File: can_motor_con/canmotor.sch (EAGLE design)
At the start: 36 parts

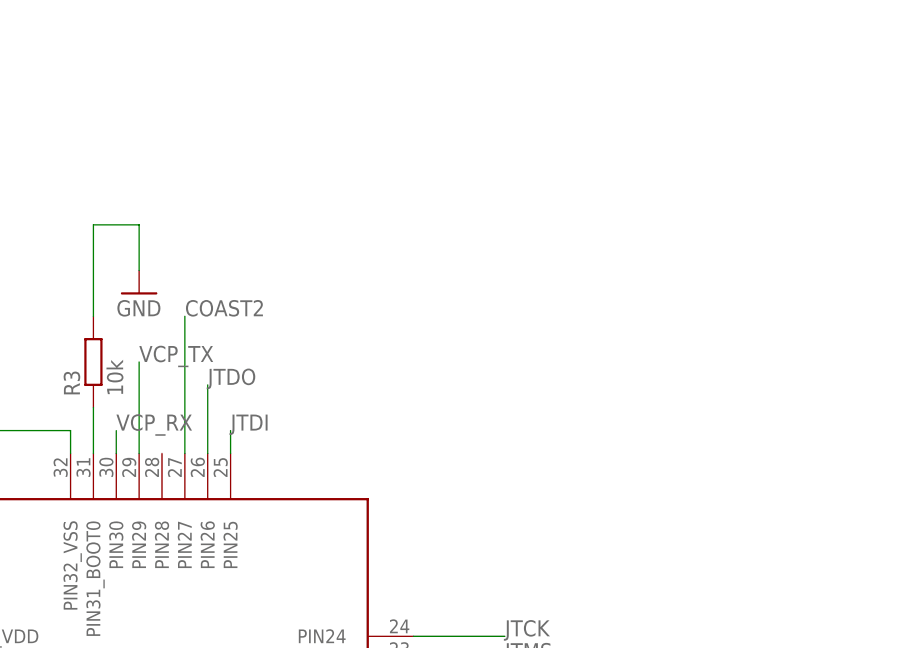
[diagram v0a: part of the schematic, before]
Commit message: ledをついか
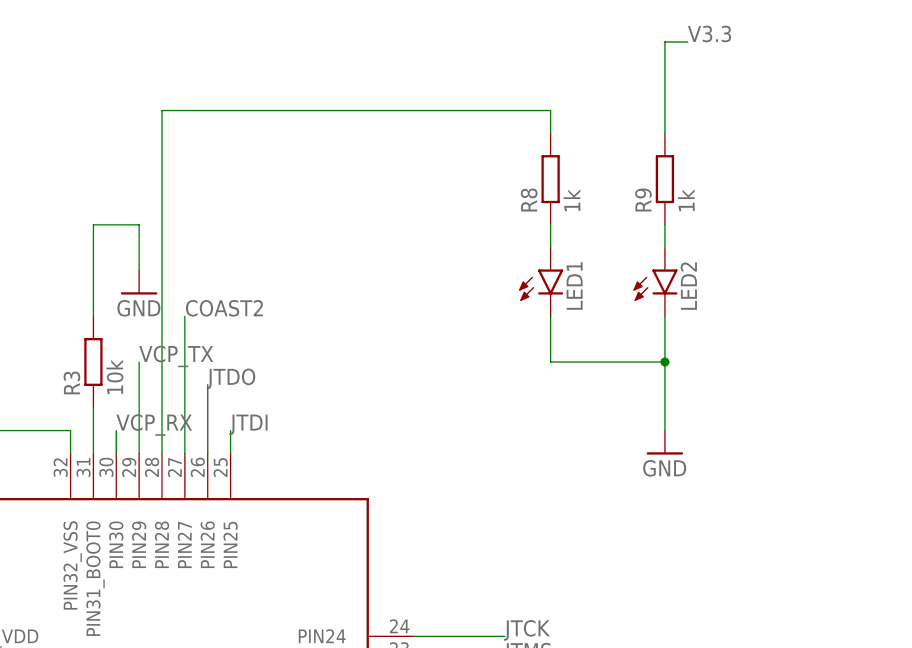
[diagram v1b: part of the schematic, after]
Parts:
- added LED1, LED2: (no value), user_leds:1608LED
- added R8, R9: 1k, user_rcl:R_REG
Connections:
- new net N$11: LED1.A, R8.1
- new net N$12: LED2.A, R9.1
- new net N$14: R8.2, U$1.PIN28
- net GND: now also LED1.K, LED2.K
- net V3.3: now also R9.2
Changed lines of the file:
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@@
 <part name="C12" library="rcl" library_urn="urn:adsk.eagle:library:334" deviceset="C-EU" device="C1608" package3d_urn="urn:adsk.eagle:package:23621/2" value="0.1u"/>
 <part name="C13" library="rcl" library_urn="urn:adsk.eagle:library:334" deviceset="C-EU" device="C1608" package3d_urn="urn:adsk.eagle:package:23621/2" value="0.1u"/>
+<part name="LED1" library="user_leds" deviceset="1608LED" device=""/>
+<part name="LED2" library="user_leds" deviceset="1608LED" device=""/>
+<part name="R8" library="user_rcl" deviceset="R_REG" device="" value="1k"/>
+<part name="R9" library="user_rcl" deviceset="R_REG" device="" value="1k"/>
+<part name="GND10" library="supply1" library_urn="urn:adsk.eagle:library:371" deviceset="GND" device=""/>
 </parts>
 <sheets>
@@
 <attribute name="NAME" x="392.176" y="35.179" size="1.778" layer="95" rot="R180"/>
 <attribute name="VALUE" x="392.176" y="40.259" size="1.778" layer="96" rot="R180"/>
+</instance>
+<instance part="LED1" gate="G$1" x="274.32" y="152.4" smashed="yes">
+<attribute name="NAME" x="277.876" y="147.828" size="1.778" layer="95" rot="R90"/>
+<attribute name="VALUE" x="280.035" y="147.828" size="1.778" layer="96" rot="R90"/>
+</instance>
+<instance part="LED2" gate="G$1" x="287.02" y="152.4" smashed="yes">
+<attribute name="NAME" x="290.576" y="147.828" size="1.778" layer="95" rot="R90"/>
+<attribute name="VALUE" x="292.735" y="147.828" size="1.778" layer="96" rot="R90"/>
+</instance>
+<instance part="R8" gate="G$1" x="274.32" y="162.56" smashed="yes" rot="R90">
+<attribute name="NAME" x="272.8214" y="158.75" size="1.778" layer="95" rot="R90"/>
+<attribute name="VALUE" x="277.622" y="158.75" size="1.778" layer="96" rot="R90"/>
+</instance>
+<instance part="R9" gate="G$1" x="287.02" y="162.56" smashed="yes" rot="R90">
+<attribute name="NAME" x="285.5214" y="158.75" size="1.778" layer="95" rot="R90"/>
+<attribute name="VALUE" x="290.322" y="158.75" size="1.778" layer="96" rot="R90"/>
+</instance>
+<instance part="GND10" gate="1" x="287.02" y="132.08" smashed="yes">
+<attribute name="VALUE" x="284.48" y="129.54" size="1.778" layer="96"/>
 </instance>
 </instances>
@@
 <junction x="358.14" y="114.3"/>
 <label x="358.14" y="127" size="1.778" layer="95"/>
+</segment>
+<segment>
+<pinref part="R9" gate="G$1" pin="2"/>
+<wire x1="287.02" y1="167.64" x2="287.02" y2="177.8" width="0.1524" layer="91"/>
+<wire x1="287.02" y1="177.8" x2="289.56" y2="177.8" width="0.1524" layer="91"/>
+<label x="289.56" y="177.8" size="1.778" layer="95"/>
 </segment>
 </net>
@@
 <junction x="353.06" y="25.4"/>
 </segment>
+<segment>
+<pinref part="GND10" gate="1" pin="GND"/>
+<wire x1="287.02" y1="134.62" x2="287.02" y2="142.24" width="0.1524" layer="91"/>
+<pinref part="LED1" gate="G$1" pin="K"/>
+<wire x1="274.32" y1="147.32" x2="274.32" y2="142.24" width="0.1524" layer="91"/>
+<wire x1="274.32" y1="142.24" x2="287.02" y2="142.24" width="0.1524" layer="91"/>
+<pinref part="LED2" gate="G$1" pin="K"/>
+<wire x1="287.02" y1="142.24" x2="287.02" y2="147.32" width="0.1524" layer="91"/>
+<junction x="287.02" y="142.24"/>
+</segment>
 </net>
 <net name="VCC" class="0">
@@
 </segment>
 </net>
+<net name="N$11" class="0">
+<segment>
+<pinref part="LED1" gate="G$1" pin="A"/>
+<pinref part="R8" gate="G$1" pin="1"/>
+<wire x1="274.32" y1="154.94" x2="274.32" y2="157.48" width="0.1524" layer="91"/>
+</segment>
+</net>
+<net name="N$12" class="0">
+<segment>
+<pinref part="LED2" gate="G$1" pin="A"/>
+<pinref part="R9" gate="G$1" pin="1"/>
+<wire x1="287.02" y1="154.94" x2="287.02" y2="157.48" width="0.1524" layer="91"/>
+</segment>
+</net>
+<net name="N$14" class="0">
+<segment>
+<pinref part="R8" gate="G$1" pin="2"/>
+<wire x1="274.32" y1="167.64" x2="274.32" y2="170.18" width="0.1524" layer="91"/>
+<wire x1="274.32" y1="170.18" x2="231.14" y2="170.18" width="0.1524" layer="91"/>
+<pinref part="U$1" gate="G$1" pin="PIN28"/>
+<wire x1="231.14" y1="170.18" x2="231.14" y2="132.08" width="0.1524" layer="91"/>
+</segment>
+</net>

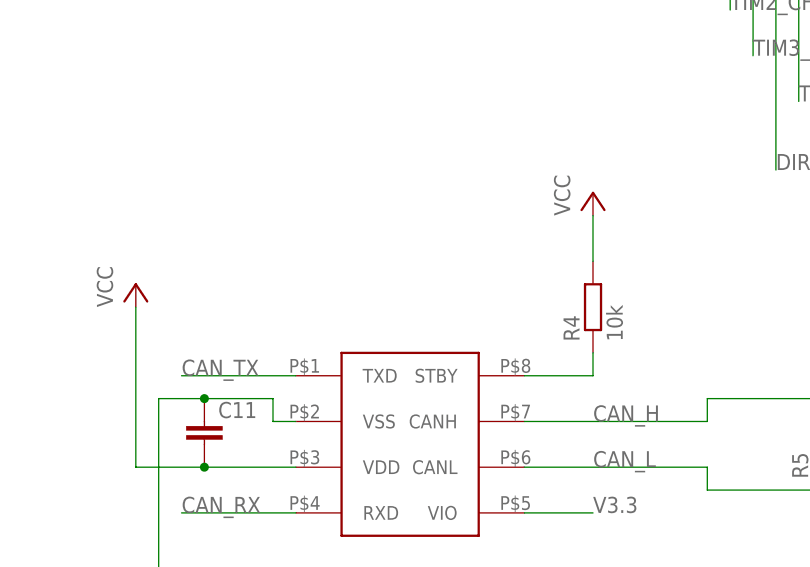
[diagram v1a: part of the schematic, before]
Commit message: mcp2562スタンバイピンプルダウン
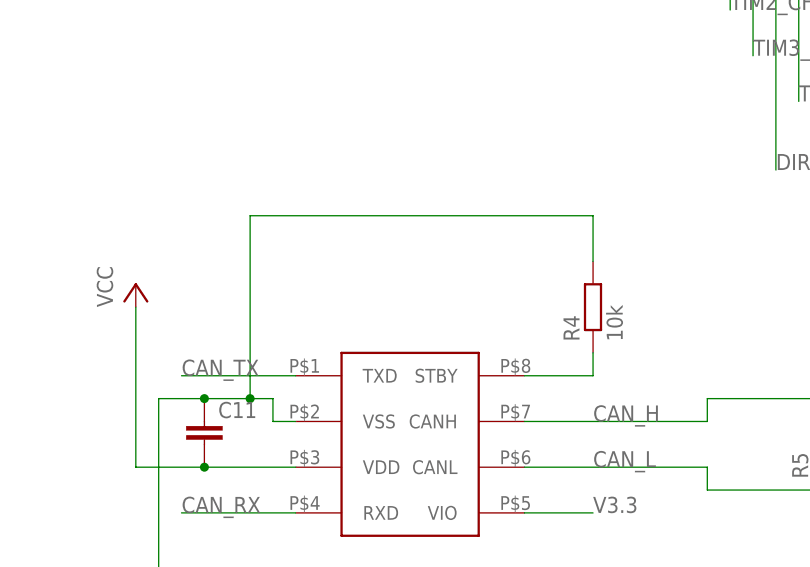
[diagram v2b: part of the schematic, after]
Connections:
- net GND: now also R4.2
- net VCC: no longer R4.2
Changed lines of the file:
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@@
 <part name="P+3" library="supply1" library_urn="urn:adsk.eagle:library:371" deviceset="VCC" device=""/>
 <part name="R4" library="user_rcl" deviceset="R_REG" device="" value="10k"/>
-<part name="P+4" library="supply1" library_urn="urn:adsk.eagle:library:371" deviceset="VCC" device=""/>
 <part name="R5" library="user_rcl" deviceset="R_REG" device="" value="120"/>
 <part name="U$6" library="user_conector" deviceset="BOX14P" device=""/>
@@
 <attribute name="VALUE" x="209.042" y="31.75" size="1.778" layer="96" rot="R90"/>
 </instance>
-<instance part="P+4" gate="VCC" x="205.74" y="48.26" smashed="yes">
-<attribute name="VALUE" x="203.2" y="45.72" size="1.778" layer="96" rot="R90"/>
-</instance>
 <instance part="R5" gate="G$1" x="231.14" y="20.32" smashed="yes" rot="R90">
 <attribute name="NAME" x="229.6414" y="16.51" size="1.778" layer="95" rot="R90"/>
@@
 <pinref part="C11" gate="G$1" pin="1"/>
 <wire x1="157.48" y1="25.4" x2="162.56" y2="25.4" width="0.1524" layer="91"/>
-<wire x1="162.56" y1="25.4" x2="170.18" y2="25.4" width="0.1524" layer="91"/>
+<wire x1="162.56" y1="25.4" x2="167.64" y2="25.4" width="0.1524" layer="91"/>
 <junction x="162.56" y="25.4"/>
+<wire x1="167.64" y1="25.4" x2="170.18" y2="25.4" width="0.1524" layer="91"/>
 <wire x1="170.18" y1="25.4" x2="170.18" y2="22.86" width="0.1524" layer="91"/>
 <pinref part="U$5" gate="G$1" pin="VSS"/>
 <wire x1="170.18" y1="22.86" x2="172.72" y2="22.86" width="0.1524" layer="91"/>
+<pinref part="R4" gate="G$1" pin="2"/>
+<wire x1="205.74" y1="40.64" x2="205.74" y2="45.72" width="0.1524" layer="91"/>
+<wire x1="205.74" y1="45.72" x2="167.64" y2="45.72" width="0.1524" layer="91"/>
+<wire x1="167.64" y1="45.72" x2="167.64" y2="25.4" width="0.1524" layer="91"/>
+<junction x="167.64" y="25.4"/>
 </segment>
 <segment>
@@
 <junction x="162.56" y="17.78"/>
 </segment>
-<segment>
-<pinref part="P+4" gate="VCC" pin="VCC"/>
-<pinref part="R4" gate="G$1" pin="2"/>
-<wire x1="205.74" y1="45.72" x2="205.74" y2="40.64" width="0.1524" layer="91"/>
-</segment>
 </net>
